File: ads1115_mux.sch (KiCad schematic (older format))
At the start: 3 parts, among them U2 ADS1115IDGST, U3 CD74HC4067M

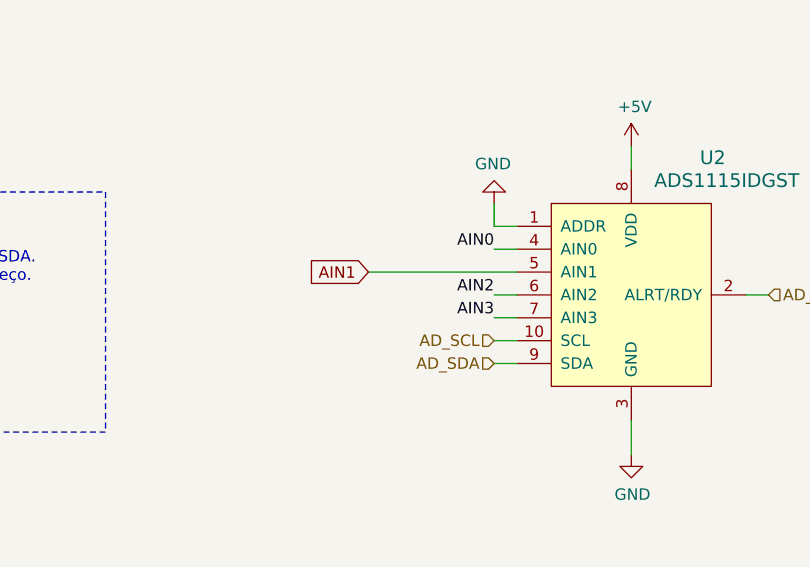
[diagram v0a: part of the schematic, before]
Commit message: Adicionando radio LoRa. Criando um .sch para a Raspberry e para o radio
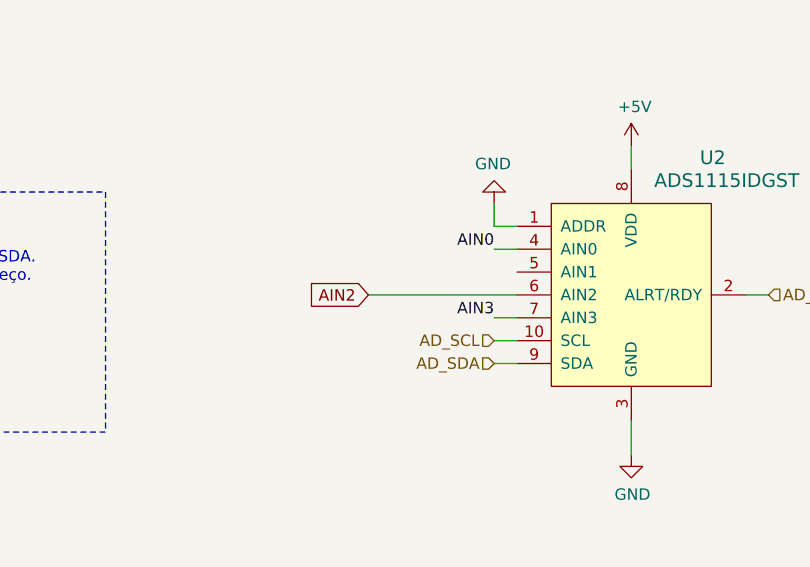
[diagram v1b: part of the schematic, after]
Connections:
- net AIN1: no longer names the net of U2.5 (AIN1)
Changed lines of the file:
@@
 $Descr A4 11693 8268
 encoding utf-8
-Sheet 3 5
+Sheet 3 7
 Title ""
 Date "2021-12-26"
@@
 Text Label 4600 3450 2    50   ~ 0
 AIN0
-Wire Wire Line
-	4700 3650 4600 3650
 $Comp
 L dk_Data-Acquisition-Analog-to-Digital-Converters-ADC:ADS1115IDGST U2
@@
 	1    0    0    -1
 $EndComp
-Text Label 4600 3650 2    50   ~ 0
-AIN2
 Text Label 4600 3750 2    50   ~ 0
 AIN3
@@
 Text HLabel 8800 4400 2    50   Input ~ 0
 I15
-Text GLabel 4050 3550 0    50   Input ~ 0
-AIN1
-Wire Wire Line
-	4050 3550 4700 3550
+Text GLabel 4050 3650 0    50   Input ~ 0
+AIN2
+Wire Wire Line
+	4050 3650 4700 3650
 Wire Wire Line
 	8200 2550 8200 2600
@@
 AD_SCL
 $Comp
-L power:+5V #PWR?
+L power:+5V #PWR0139
 U 1 1 61DBE0C8
 P 6100 1700
-F 0 "#PWR?" H 6100 1550 50  0001 C CNN
+F 0 "#PWR0139" H 6100 1550 50  0001 C CNN
 F 1 "+5V" H 6115 1873 50  0000 C CNN
 F 2 "" H 6100 1700 50  0001 C CNN
@@
 $EndComp
 $Comp
-L power:+5V #PWR?
+L power:+5V #PWR0140
 U 1 1 61DBF330
 P 8200 2550
-F 0 "#PWR?" H 8200 2400 50  0001 C CNN
+F 0 "#PWR0140" H 8200 2400 50  0001 C CNN
 F 1 "+5V" H 8215 2723 50  0000 C CNN
 F 2 "" H 8200 2550 50  0001 C CNN
@@
 $EndComp
 $Comp
-L power:+5V #PWR?
+L power:+5V #PWR0141
 U 1 1 61DBF85C
 P 5200 3000
-F 0 "#PWR?" H 5200 2850 50  0001 C CNN
+F 0 "#PWR0141" H 5200 2850 50  0001 C CNN
 F 1 "+5V" H 5215 3173 50  0000 C CNN
 F 2 "" H 5200 3000 50  0001 C CNN
